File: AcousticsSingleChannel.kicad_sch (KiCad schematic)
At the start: 22 parts, among them J1 Conn_01x04_Pin, J2 Conn_01x04_Pin, J4 Conn_01x09_Pin, U1 OPA1604AIPWR, U2 ADS127L21IRUKT

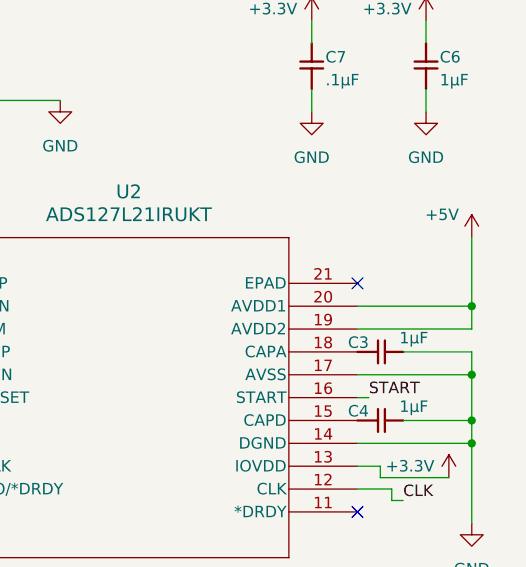
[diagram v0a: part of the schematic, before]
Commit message: Layer Stackup Updates.
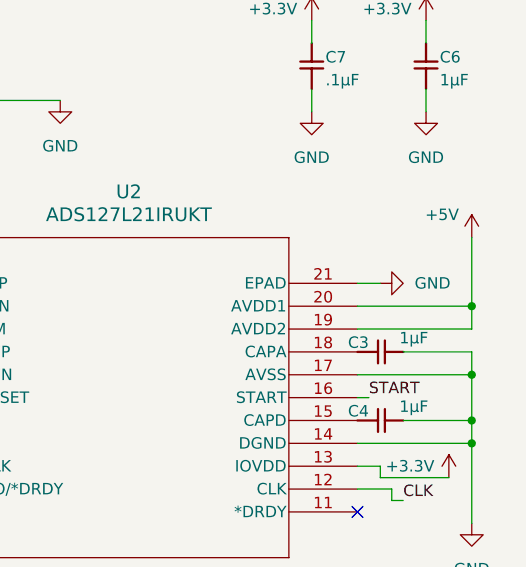
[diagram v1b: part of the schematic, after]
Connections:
- net GND: now also U2.21 (EPAD)
- no-connect marks 3 -> 2
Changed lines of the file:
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@@
 		(at 251.46 119.38)
 	)
-	(no_connect
-		(at 251.46 93.98)
-	)
 	(wire
 		(pts
@@
 		(pts
 			(xy 20.32 111.76) (xy 35.56 111.76)
+		)
+		(stroke
+			(width 0)
+			(type default)
+		)
+	)
+	(wire
+		(pts
+			(xy 251.46 93.98) (xy 254 93.98)
 		)
 		(stroke
@@
 					(unit 1)
 				)
+			)
+		)
+	)
+	(symbol
+		(lib_id "power:GND")
+		(at 254 93.98 90)
+		(unit 1)
+		(exclude_from_sim no)
+		(in_bom yes)
+		(on_board yes)
+		(dnp no)
+		(fields_autoplaced yes)
+		(property "Reference" "#PWR038"
+			(at 260.35 93.98 0)
+			(effects
+				(font
+					(size 1.27 1.27)
+				)
+				(hide yes)
+			)
+		)
+		(property "Value" "GND"
+			(at 257.81 93.9799 90)
+			(effects
+				(font
+					(size 1.27 1.27)
+				)
+				(justify right)
+			)
+		)
+		(property "Footprint" ""
+			(at 254 93.98 0)
+			(effects
+				(font
+					(size 1.27 1.27)
+				)
+				(hide yes)
+			)
+		)
+		(property "Datasheet" ""
+			(at 254 93.98 0)
+			(effects
+				(font
+					(size 1.27 1.27)
+				)
+				(hide yes)
+			)
+		)
+		(property "Description" "Power symbol creates a global label with name \"GND\" , ground"
+			(at 254 93.98 0)
+			(effects
+				(font
+					(size 1.27 1.27)
+				)
+				(hide yes)
+			)
+		)
+		(pin "1"
+		)
+		(instances
+			(project "AcousticsSingleChannel"
+				(path "/8b2368f6-513e-479c-aa25-8a2dd439cbb4"
+					(reference "#PWR038")
+					(unit 1)
+				)
